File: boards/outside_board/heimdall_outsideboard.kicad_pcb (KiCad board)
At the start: 2 copper layers, 41.7 x 44.5 mm, 11 parts, among them J1 Conn_01x09, J2 Conn_01x06, Q1 2N3904, Q2 2N7000

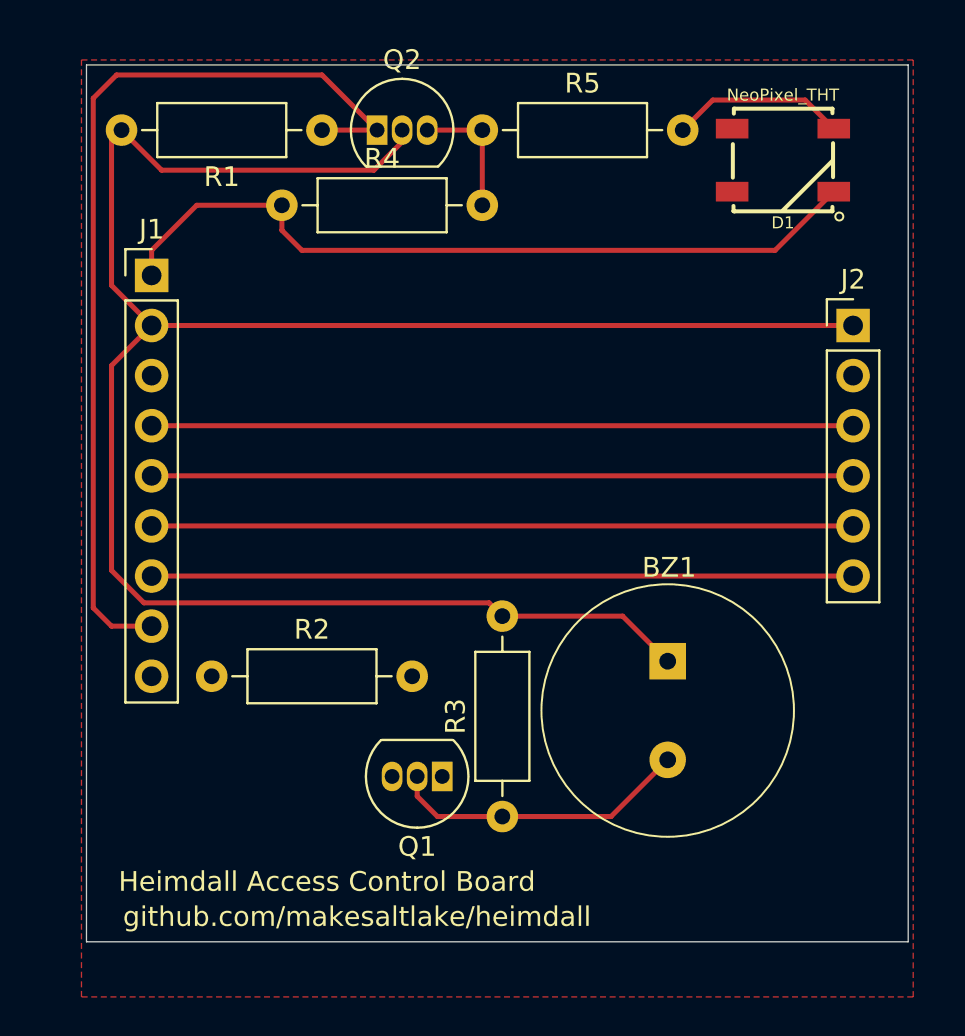
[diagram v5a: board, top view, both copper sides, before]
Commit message: Update outside board to rev 01 and add Gerber files and BOM.
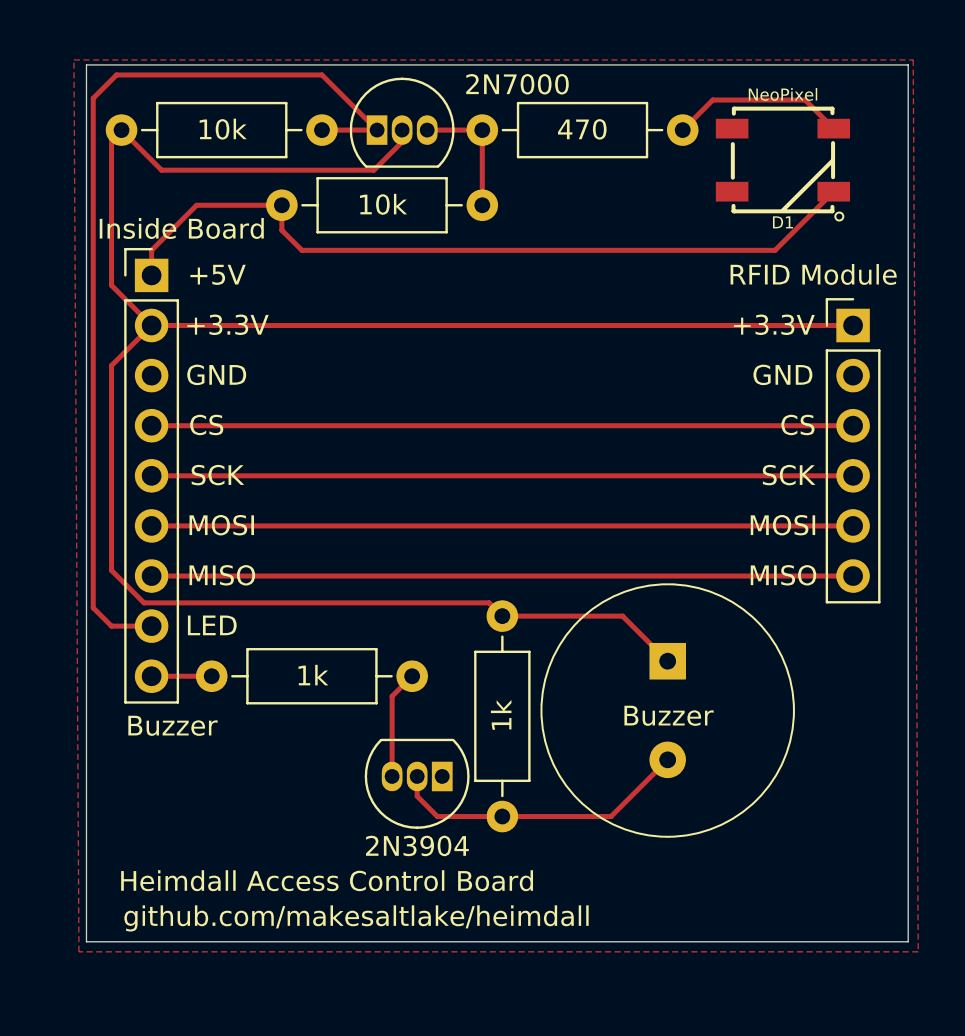
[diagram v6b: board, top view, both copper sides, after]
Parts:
- D1: value NeoPixel_THT -> NeoPixel
- Inside Board: renamed from J1
- RFID Module: renamed from J2
- renumbered R1 to 10k, R4 to 10k, R2 to 1k, R3 to 1k, Q1 to 2N3904, Q2 to 2N7000, R5 to 470, BZ1 to Buzzer
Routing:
- net Net-(Q1-Pad3): track 0.00 -> 5.50 mm
- net /Buzzer: track 0.00 -> 3.05 mm
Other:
- board text added: "+3.3V"
- board text added: "+5V"
- board text added: "Buzzer"
- board text added: "CS"
- board text added: "GND"
- board text added: "LED"
- board text added: "MISO"
- board text added: "MOSI"
- board text added: "SCK"

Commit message: Update outside board schematics and layout to revision 2
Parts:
- removed 2N3904: 2N3904, Package_TO_SOT_THT:TO-92_Inline
- added J3: Conn_01x01_Male, Connector_PinHeader_2.54mm:PinHeader_1x01_P2.54mm_Vertical, F.Cu at (77.2, 104.6)
- added J4: Conn_01x01_Male, Connector_PinHeader_2.54mm:PinHeader_1x01_P2.54mm_Vertical, F.Cu at (76.5, 113.8)
- added J5: Conn_01x01_Male, Connector_PinHeader_2.54mm:PinHeader_1x01_P2.54mm_Vertical, F.Cu at (83.6, 83.1)
- added J6: Conn_01x01_Male, Connector_PinHeader_2.54mm:PinHeader_1x01_P2.54mm_Vertical, F.Cu at (78.5, 85.6)
- added Q1: 2N3904, Package_TO_SOT_THT:TO-92_Inline, F.Cu at (65.0, 112.8)
- D1: value NeoPixel -> NeoPixel_THT; footprint LED:WS2812B -> LED_THT:LED_D5.0mm-4_RGB
- J1: renamed from Inside Board
- J2: renamed from RFID Module
- moved BZ1 5.80 mm to (85.3, 109.2)
- moved D1 4.83 mm to (90.9, 81.0)
- renumbered Buzzer to BZ1, 2N7000 to Q2, 10k to R1, 1k to R2, 1k to R3, 10k to R4, 470 to R5
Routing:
- net +3V3: track 106.1 -> 112.4 mm
- net Net-(BZ1-Pad2): track 15.3 -> 18.9 mm
- net Net-(D1-Pad4): track 8.89 -> 10.2 mm
- net +5V: track 39.7 -> 40.9 mm
- net Net-(Q1-Pad2): track 5.50 -> 6.01 mm
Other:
- net class Default: clearance 0.2032 -> 0.1524
- rule trace_clearance: 0.2032 -> 0.1524
- rule trace_min: 0.1524 -> 0.1016
